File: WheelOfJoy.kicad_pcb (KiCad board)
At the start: 2 copper layers, 89.2 x 87.9 mm, 39 parts, among them CN1 JOY1, CN2 JOY2, CN3 JOY3, CN4 JOY4, CN5 JOY5, CN6 JOY6, CN7 JOY7, CN8 JOY8, CN9 DB15F, U1 CD4051B, U2 CD4051B, U3 CD4051B, U4 CD4051B, U5 CD4051B

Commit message: WIP
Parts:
- removed C4, C5: 100n, Capacitor_THT:C_Disc_D7.0mm_W2.5mm_P5.00mm
- removed CN5: JOY5, Connector_Dsub:DSUB-9_Male_EdgeMount_P2.77mm
- removed CN6: JOY6, Connector_Dsub:DSUB-9_Male_EdgeMount_P2.77mm
- removed CN7: JOY7, Connector_Dsub:DSUB-9_Male_EdgeMount_P2.77mm
- removed CN8: JOY8, Connector_Dsub:DSUB-9_Male_EdgeMount_P2.77mm
- removed RN9: 100, Resistor_THT:R_Array_SIP10
- removed U4, U5: CD4051B, Package_DIP:DIP-16_W7.62mm_Socket_LongPads
- removed V6: PORT5_NO, WheelOfJoy:port5
- removed V7: PORT6_NO, WheelOfJoy:port6
- removed V8: PORT7_NO, WheelOfJoy:port7
- removed V9: PORT8_NO, WheelOfJoy:port8
- C1, C2, C3: footprint Capacitor_THT:C_Disc_D7.0mm_W2.5mm_P5.00mm -> Capacitor_SMD:C_0805_2012Metric_Pad1.18x1.45mm_HandSolder; moved to B.Cu
- C6: footprint Capacitor_THT:CP_Radial_D6.3mm_P2.50mm -> Capacitor_SMD:C_1206_3216Metric_Pad1.33x1.80mm_HandSolder
- RN1, RN2, RN3, RN4, RN5, RN6: footprint Resistor_THT:R_Array_SIP6 -> Resistor_SMD:R_Array_Convex_4x0603; moved to B.Cu
- RN7, RN8: value 4.7k -> 100; footprint Resistor_THT:R_Array_SIP6 -> Resistor_SMD:R_Array_Convex_4x0603
- U1, U2, U3: value CD4051B -> 74LS153; footprint Package_DIP:DIP-16_W7.62mm_Socket_LongPads -> Package_SO:SOIC-16_3.9x9.9mm_P1.27mm; moved to B.Cu
- moved V5 80.0 mm to (166.0, 130.4)
- moved CN4 72.9 mm to (167.4, 121.2), turned to 77.2 degrees
- moved RN4 63.6 mm to (148.6, 124.4), turned to 180 degrees
- moved RN5 61.2 mm to (148.6, 119.2), turned to 180 degrees
- moved V4 61.1 mm to (166.8, 106.8)
- moved RN6 53.1 mm to (161.7, 121.2), turned to 180 degrees
- moved CN3 51.3 mm to (159.4, 100.4), turned to 144 degrees
- moved RN7 50.5 mm to (148.6, 126.9), turned to 90 degrees
- moved V0 43.8 mm to (148.8, 111.3)
- moved RN3 43.6 mm to (135.5, 121.2), turned to 180 degrees
- moved U2 41.0 mm to (141.8, 121.2), turned to 180 degrees
- moved RN8 40.4 mm to (140.1, 126.9), turned to 90 degrees
- moved C2 39.3 mm to (141.8, 114.2), turned to 0 degrees
- moved RN2 37.0 mm to (155.4, 106.4), turned to 180 degrees
- moved V3 35.4 mm to (146.4, 94.4)
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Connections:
- CN1 pad 9: (no net) -> Net-(CN1-Pad9)
- CN2 pad 9: (no net) -> Net-(CN2-Pad9)
- CN3 pad 9: (no net) -> Net-(CN3-Pad9)
- CN4 pad 9: (no net) -> Net-(CN4-Pad9)
- CN9 pad 11: /d5 -> Net-(CN9-Pad11)
- CN9 pad 14: (no net) -> Net-(CN9-Pad14)
- CN9 pad 6: (no net) -> /~reset
- CN9 pad 7: (no net) -> Net-(CN9-Pad7)
- RN1 pad 1: +5V -> Net-(CN4-Pad2)
- RN1 pad 2: Net-(CN1-Pad6) -> Net-(CN3-Pad2)
- RN1 pad 3: Net-(CN1-Pad4) -> Net-(CN2-Pad2)
- RN1 pad 4: Net-(CN1-Pad3) -> Net-(CN1-Pad2)
- RN1 pad 5: Net-(CN1-Pad2) -> +5V
- RN1 pad 6: Net-(CN1-Pad1) -> +5V
- RN2 pad 2: Net-(CN2-Pad6) -> +5V
- RN2 pad 3: Net-(CN2-Pad4) -> +5V
- RN2 pad 4: Net-(CN2-Pad3) -> +5V
- RN2 pad 5: Net-(CN2-Pad2) -> Net-(CN1-Pad1)
- RN3 pad 1: +5V -> Net-(CN4-Pad4)
- RN3 pad 2: Net-(CN3-Pad6) -> Net-(CN3-Pad4)
- RN3 pad 3: Net-(CN3-Pad4) -> Net-(CN2-Pad4)
- RN3 pad 4: Net-(CN3-Pad3) -> Net-(CN1-Pad4)
- RN3 pad 5: Net-(CN3-Pad2) -> +5V
- RN3 pad 6: Net-(CN3-Pad1) -> +5V
- RN4 pad 2: Net-(CN4-Pad6) -> +5V
- RN4 pad 3: Net-(CN4-Pad4) -> +5V
- RN4 pad 4: Net-(CN4-Pad3) -> +5V
- RN4 pad 5: Net-(CN4-Pad2) -> Net-(CN1-Pad3)
- RN4 pad 6: Net-(CN4-Pad1) -> Net-(CN2-Pad3)
- RN5 pad 1: +5V -> Net-(CN4-Pad9)
- RN5 pad 2: Net-(CN5-Pad6) -> Net-(CN3-Pad9)
- RN5 pad 3: Net-(CN5-Pad4) -> Net-(CN2-Pad9)
- RN5 pad 4: Net-(CN5-Pad3) -> Net-(CN1-Pad9)
- RN5 pad 5: Net-(CN5-Pad2) -> +5V
- RN5 pad 6: Net-(CN5-Pad1) -> +5V
- RN6 pad 2: Net-(CN6-Pad6) -> +5V
- RN6 pad 3: Net-(CN6-Pad4) -> +5V
- RN6 pad 4: Net-(CN6-Pad3) -> +5V
- RN6 pad 5: Net-(CN6-Pad2) -> Net-(CN1-Pad6)
- RN6 pad 6: Net-(CN6-Pad1) -> Net-(CN2-Pad6)
- RN7 pad 1: +5V -> Net-(RN7-Pad1)
- RN7 pad 3: Net-(CN7-Pad4) -> Net-(CN9-Pad11)
- RN7 pad 4: Net-(CN7-Pad3) -> Net-(CN9-Pad10)
- RN7 pad 5: Net-(CN7-Pad2) -> /d4
- RN7 pad 6: Net-(CN7-Pad1) -> /d5
- RN8 pad 1: +5V -> Net-(CN9-Pad5)
- RN8 pad 2: Net-(CN8-Pad6) -> Net-(CN9-Pad4)
- RN8 pad 3: Net-(CN8-Pad4) -> Net-(CN9-Pad3)
- RN8 pad 4: Net-(CN8-Pad3) -> Net-(CN9-Pad2)
- RN8 pad 5: Net-(CN8-Pad2) -> /d0
- RN8 pad 6: Net-(CN8-Pad1) -> /d1
- U1 pad 1: Net-(CN5-Pad1) -> GND
- U1 pad 10: /d6 -> Net-(CN1-Pad2)
- U1 pad 11: /d5 -> Net-(CN2-Pad2)
- U1 pad 12: Net-(CN4-Pad1) -> Net-(CN3-Pad2)
- U1 pad 13: Net-(CN1-Pad1) -> Net-(CN4-Pad2)
- U1 pad 14: Net-(CN2-Pad1) -> /d6
- U1 pad 15: Net-(CN3-Pad1) -> GND
- U1 pad 2: Net-(CN7-Pad1) -> /d7
- U1 pad 3: /d0 -> Net-(CN4-Pad1)
- U1 pad 4: Net-(CN8-Pad1) -> Net-(CN3-Pad1)
- U1 pad 5: Net-(CN6-Pad1) -> Net-(CN2-Pad1)
- U1 pad 6: GND -> Net-(CN1-Pad1)
- U1 pad 7: GND -> /d0
- U1 pad 9: /d7 -> /d1
- U2 pad 1: Net-(CN5-Pad2) -> GND
- U2 pad 10: /d6 -> Net-(CN1-Pad4)
- U2 pad 11: /d5 -> Net-(CN2-Pad4)
- U2 pad 12: Net-(CN4-Pad2) -> Net-(CN3-Pad4)
- U2 pad 13: Net-(CN1-Pad2) -> Net-(CN4-Pad4)
- U2 pad 14: Net-(CN2-Pad2) -> /d6
- U2 pad 15: Net-(CN3-Pad2) -> GND
- U2 pad 2: Net-(CN7-Pad2) -> /d7
- U2 pad 3: /d1 -> Net-(CN4-Pad3)
- U2 pad 4: Net-(CN8-Pad2) -> Net-(CN3-Pad3)
- U2 pad 5: Net-(CN6-Pad2) -> Net-(CN2-Pad3)
- U2 pad 6: GND -> Net-(CN1-Pad3)
- U2 pad 7: GND -> /d2
- U2 pad 9: /d7 -> /d3
- U3 pad 1: Net-(CN5-Pad3) -> GND
- U3 pad 10: /d6 -> Net-(CN1-Pad9)
- U3 pad 11: /d5 -> Net-(CN2-Pad9)
- U3 pad 12: Net-(CN4-Pad3) -> Net-(CN3-Pad9)
- U3 pad 13: Net-(CN1-Pad3) -> Net-(CN4-Pad9)
- U3 pad 14: Net-(CN2-Pad3) -> /d6
- U3 pad 15: Net-(CN3-Pad3) -> GND
- U3 pad 2: Net-(CN7-Pad3) -> /d7
- U3 pad 3: /d2 -> Net-(CN4-Pad6)
- U3 pad 4: Net-(CN8-Pad3) -> Net-(CN3-Pad6)
- U3 pad 5: Net-(CN6-Pad3) -> Net-(CN2-Pad6)
- U3 pad 6: GND -> Net-(CN1-Pad6)
- U3 pad 7: GND -> /d4
- U3 pad 9: /d7 -> /d5
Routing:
- net +5V: track 461.8 -> 66.4 mm, vias 6 -> 1
- net /d5: track 134.9 -> 0.00 mm, vias 2 -> 0
- net /d6: track 131.0 -> 0.00 mm, vias 2 -> 0
- net /d7: track 134.7 -> 14.2 mm, vias 1 -> 0
- net Net-(CN5-Pad6): track 84.9 -> 0.00 mm, vias 1 -> 0
- net Net-(CN1-Pad2): track 86.5 -> 3.99 mm, vias 1 -> 0
- net Net-(CN6-Pad6): track 81.6 -> 0.00 mm, vias 3 -> 0
- net Net-(CN7-Pad1): track 79.7 -> 0.00 mm, vias 1 -> 0
- net Net-(CN5-Pad3): track 79.0 -> 0.00 mm, vias 2 -> 0
- net Net-(CN6-Pad3): track 75.1 -> 0.00 mm, vias 1 -> 0
- net Net-(RN7-Pad2): track 74.6 -> 0.00 mm, vias 3 -> 0
- net Net-(CN8-Pad1): track 73.8 -> 0.00 mm, vias 1 -> 0
- net Net-(CN8-Pad3): track 67.6 -> 0.00 mm, vias 1 -> 0
- net Net-(CN3-Pad6): track 70.0 -> 3.05 mm, vias 1 -> 0
- net Net-(CN2-Pad2): track 69.1 -> 3.80 mm, vias 1 -> 0
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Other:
- board size 89.2 x 87.9 mm -> 47.8 x 45.4 mm

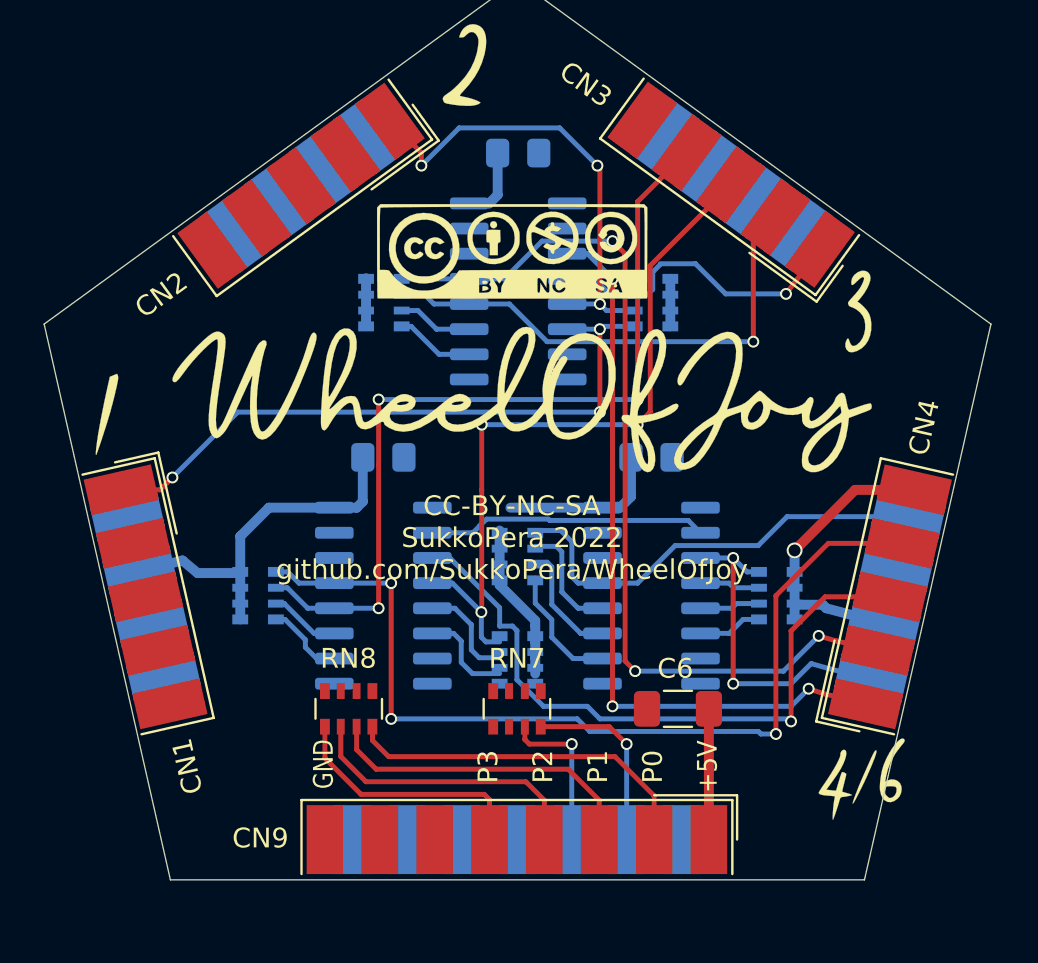
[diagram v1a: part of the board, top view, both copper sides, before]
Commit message: Restart routing from scratch
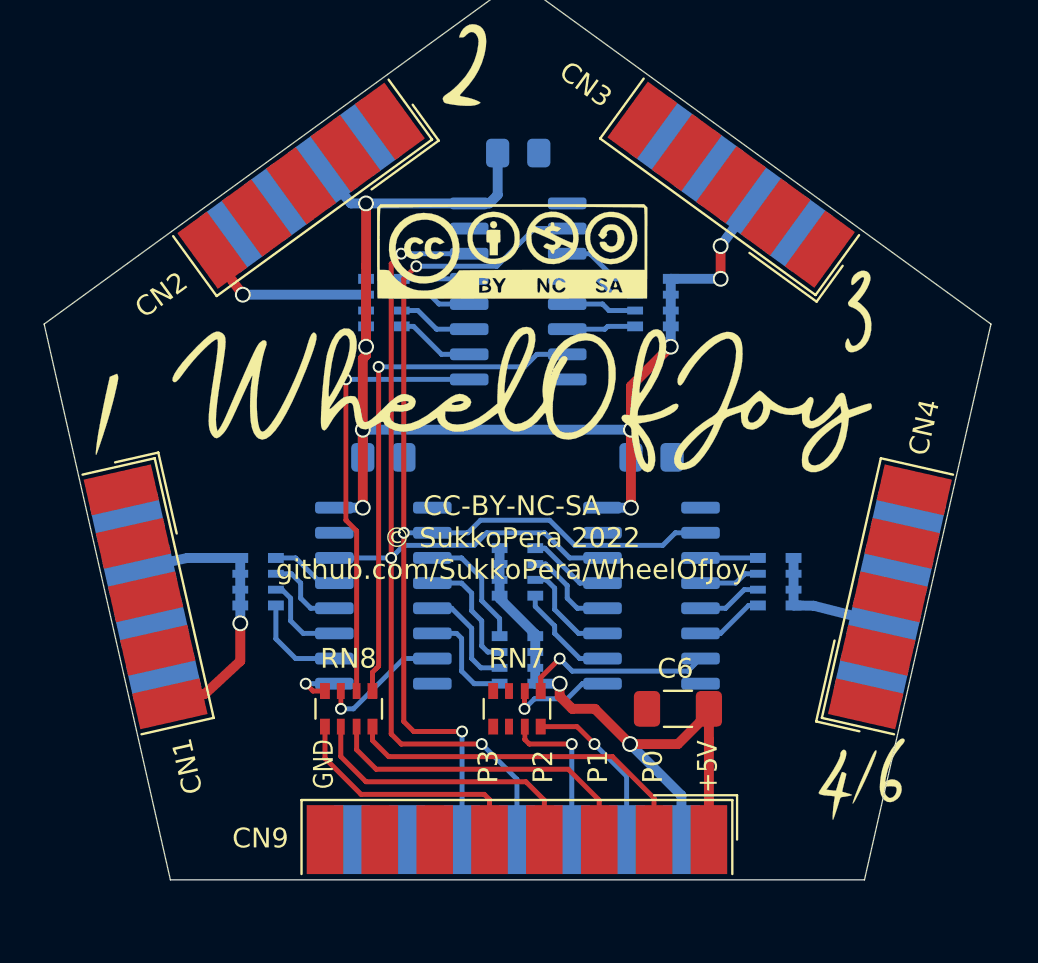
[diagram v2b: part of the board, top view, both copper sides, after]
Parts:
- moved RN5 0.77 mm to (148.6, 120.0)
- moved RN6 0.71 mm to (161.7, 120.5)
- moved RN3 0.70 mm to (135.5, 120.5)
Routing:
- net +5V: track 66.4 -> 132.0 mm, vias 1 -> 13
- net /d6: track 0.00 -> 52.8 mm, vias 0 -> 3
- net Net-(CN4-Pad4): track 47.1 -> 3.48 mm, vias 3 -> 0
- net Net-(CN4-Pad2): track 46.8 -> 3.41 mm, vias 3 -> 0
- net /d7: track 14.2 -> 56.3 mm, vias 0 -> 3
- net Net-(CN3-Pad4): track 42.9 -> 4.12 mm, vias 3 -> 0
- net Net-(CN4-Pad1): track 38.8 -> 3.96 mm, vias 3 -> 0
- net Net-(CN3-Pad3): track 36.8 -> 6.10 mm, vias 3 -> 0
- net Net-(CN1-Pad1): track 33.5 -> 3.49 mm, vias 3 -> 0
- net Net-(CN4-Pad3): track 33.8 -> 6.22 mm, vias 1 -> 0
- net /d0: track 0.00 -> 26.3 mm, vias 0 -> 1
- net /d1: track 0.00 -> 22.2 mm, vias 0 -> 1
- net Net-(CN3-Pad2): track 25.5 -> 3.60 mm, vias 1 -> 0
- net Net-(CN2-Pad1): track 24.0 -> 3.57 mm, vias 3 -> 0
- net Net-(CN4-Pad9): track 22.4 -> 4.13 mm
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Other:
- board text added: "CC-BY-NC-SA © SukkoPera 2022 github.com/SukkoPera/WheelOfJoy"
- board text removed: "CC-BY-NC-SA SukkoPera 2022 github.com/SukkoPera/WheelOfJoy"

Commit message: WIP
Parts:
- removed C2, C3: 100n, Capacitor_SMD:C_0805_2012Metric_Pad1.18x1.45mm_HandSolder
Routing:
- net +5V: track 132.0 -> 177.5 mm, vias 13 -> 23
- net Net-(CN1-Pad9): track 5.25 -> 50.2 mm, vias 0 -> 4
- net GND: track 0.00 -> 43.9 mm, vias 0 -> 6
- net Net-(CN3-Pad4): track 4.12 -> 47.8 mm, vias 0 -> 3
- net Net-(CN1-Pad6): track 3.54 -> 43.0 mm, vias 0 -> 6
- net Net-(CN4-Pad2): track 3.41 -> 42.7 mm, vias 0 -> 3
- net Net-(CN2-Pad6): track 3.34 -> 42.0 mm, vias 0 -> 4
- net Net-(CN4-Pad4): track 3.48 -> 41.7 mm, vias 0 -> 3
- net Net-(CN4-Pad3): track 6.22 -> 43.1 mm, vias 0 -> 3
- net Net-(CN3-Pad3): track 6.10 -> 38.6 mm, vias 0 -> 3
- net Net-(CN2-Pad9): track 5.15 -> 37.6 mm, vias 0 -> 4
- net Net-(CN4-Pad1): track 3.96 -> 36.3 mm, vias 0 -> 3
- net Net-(CN1-Pad1): track 3.49 -> 33.9 mm, vias 0 -> 3
- net Net-(CN2-Pad3): track 5.54 -> 34.4 mm, vias 0 -> 3
- net Net-(CN1-Pad3): track 5.42 -> 33.0 mm, vias 0 -> 3
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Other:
- net class Default: clearance 0.2 -> 0.15; trace_width 0.25 -> 0.16; via_dia 0.6 -> 0.3; via_drill 0.4 -> 0.25
- net class Power: clearance 0.2 -> 0.15
- rule trace_clearance: 0.2 -> 0.15
- rule trace_min: 0.2 -> 0.127
- rule via_min_drill: 0.3 -> 0.25
- rule via_min_size: 0.4 -> 0.3

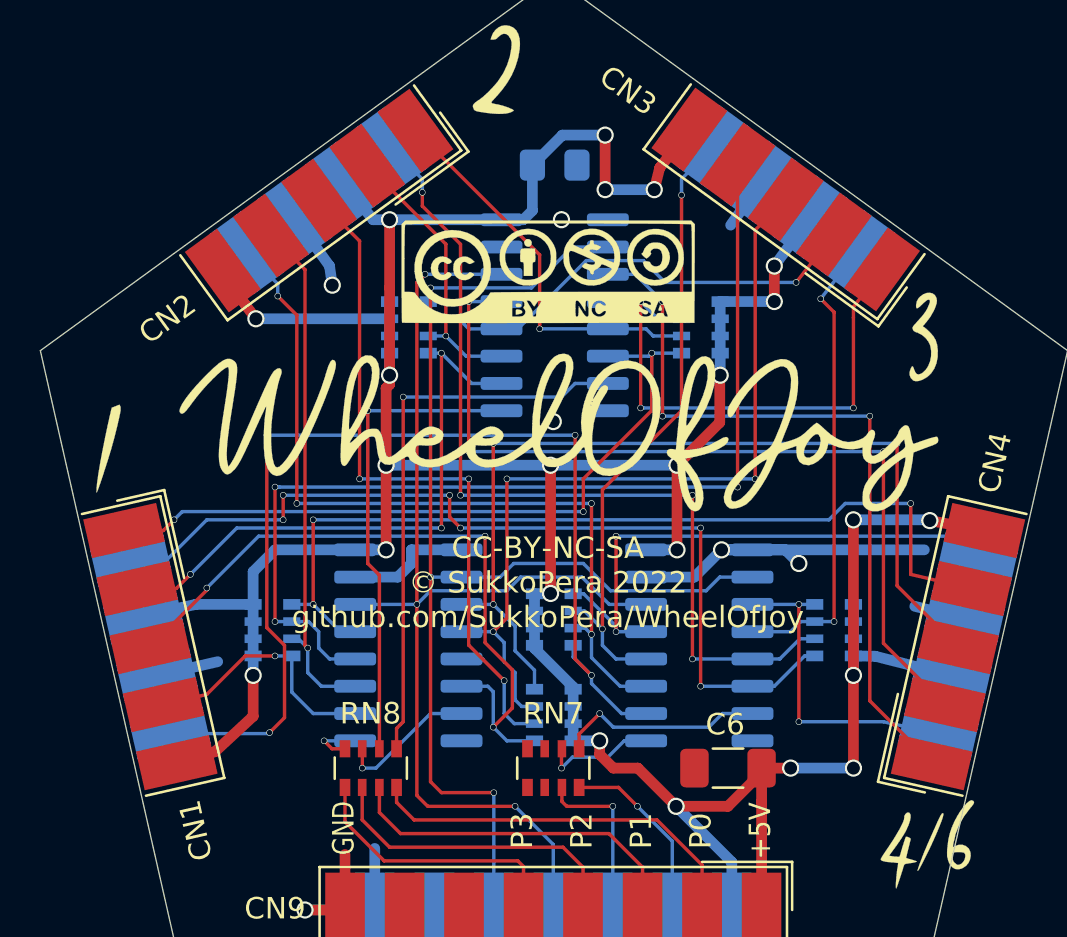
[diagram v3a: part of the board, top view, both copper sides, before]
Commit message: Honing tracks
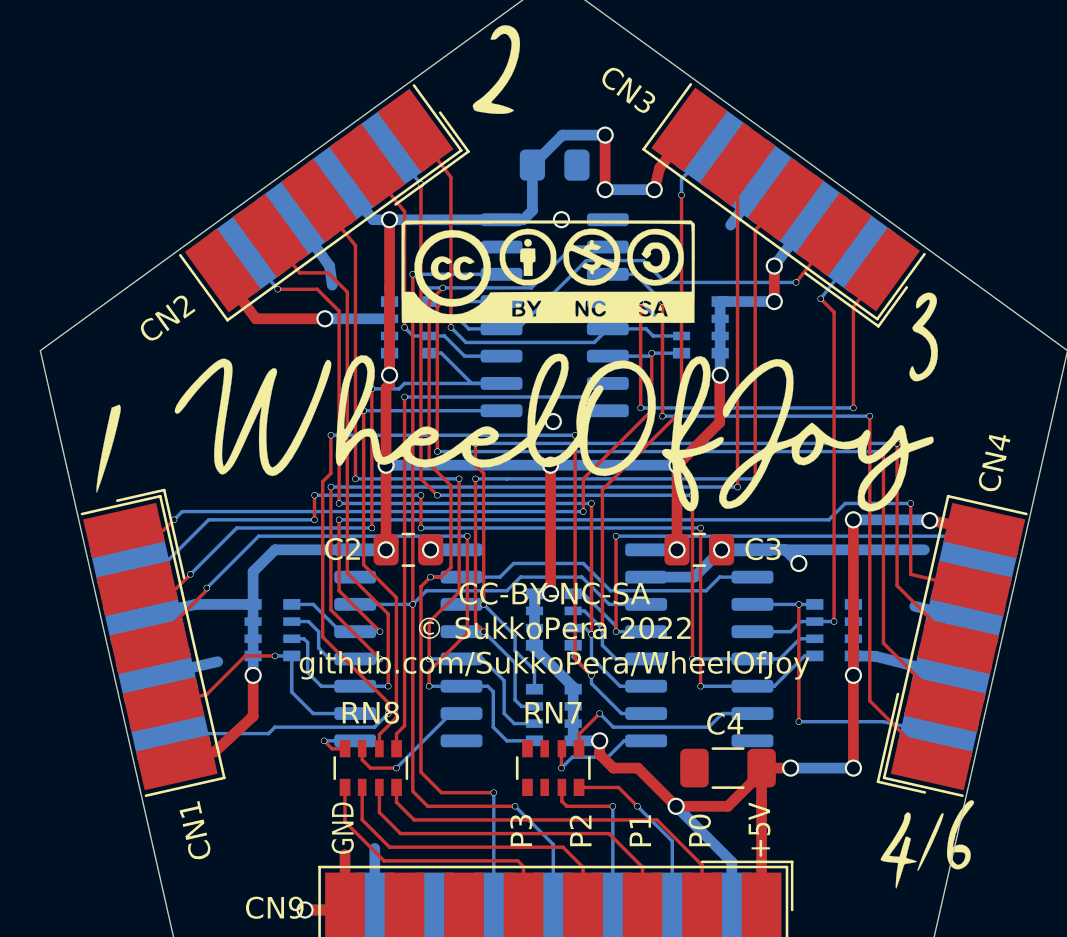
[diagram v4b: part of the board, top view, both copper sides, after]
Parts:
- added C2: 100n, Capacitor_SMD:C_0805_2012Metric_Pad1.18x1.45mm_HandSolder, F.Cu at (141.8, 116.7)
- added C3: 100n, Capacitor_SMD:C_0805_2012Metric_Pad1.18x1.45mm_HandSolder, F.Cu at (155.4, 116.7)
- moved V0 0.22 mm to (148.6, 111.3)
- renumbered C6 to C4
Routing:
- net GND: track 43.9 -> 38.0 mm
- net Net-(CN2-Pad4): track 24.4 -> 30.1 mm
- net Net-(CN1-Pad9): track 50.2 -> 53.0 mm
- net Net-(CN2-Pad1): track 18.4 -> 21.1 mm
- net /d7: track 56.7 -> 58.9 mm
- net Net-(CN4-Pad4): track 41.7 -> 43.7 mm
- net Net-(CN4-Pad2): track 42.7 -> 44.2 mm
- net Net-(CN1-Pad3): track 33.0 -> 31.6 mm
- net Net-(CN1-Pad2): track 27.5 -> 28.7 mm
- net Net-(CN3-Pad3): track 38.6 -> 39.7 mm
- net /d1: track 22.2 -> 23.1 mm
- net Net-(CN4-Pad3): track 43.1 -> 43.9 mm
- net Net-(CN2-Pad6): track 42.0 -> 42.6 mm

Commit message: Another port done
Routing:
- net Net-(CN1-Pad4): track 11.8 -> 32.5 mm, vias 1 -> 3
- net Net-(CN1-Pad9): track 53.0 -> 48.6 mm, vias 4 -> 6
- net Net-(CN1-Pad6): track 43.3 -> 40.3 mm, vias 6 -> 2
- net Net-(CN1-Pad3): track 31.6 -> 33.9 mm
- net Net-(CN1-Pad2): track 28.7 -> 29.5 mm
- net +5V: track 177.6 -> 178.2 mm

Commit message: Another one
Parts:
- C1: moved to F.Cu
- moved C1 2.54 mm to (148.7, 101.3)
- moved V1 1.42 mm to (148.6, 105.2)
- moved V0 0.76 mm to (148.6, 112.0)
- moved V4 0.57 mm to (167.3, 106.6)
- moved V3 0.51 mm to (146.4, 94.9)
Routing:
- net Net-(CN3-Pad1): track 25.5 -> 15.8 mm
- net GND: track 38.0 -> 30.0 mm
- net Net-(CN2-Pad9): track 37.4 -> 44.1 mm
- net Net-(CN1-Pad9): track 48.6 -> 54.8 mm
- net Net-(CN3-Pad6): track 22.1 -> 28.0 mm
- net Net-(CN4-Pad6): track 15.0 -> 20.3 mm
- net Net-(CN1-Pad1): track 33.9 -> 37.2 mm
- net Net-(CN3-Pad9): track 29.3 -> 32.6 mm
- net Net-(CN3-Pad4): track 48.3 -> 45.2 mm
- net Net-(CN4-Pad4): track 43.7 -> 41.2 mm
- net Net-(CN1-Pad2): track 29.5 -> 27.2 mm
- net Net-(CN4-Pad9): track 26.0 -> 28.2 mm
- net Net-(CN3-Pad3): track 39.7 -> 37.8 mm
- net Net-(CN4-Pad1): track 36.3 -> 37.6 mm
- net Net-(CN2-Pad6): track 42.6 -> 43.3 mm
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
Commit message: Almost there
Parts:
- moved RN1 1.28 mm to (141.7, 105.1)
- moved RN2 1.27 mm to (155.5, 105.1)
- moved C1 1.27 mm to (148.7, 100.1)
- moved U1 1.27 mm to (148.7, 104.5)
- moved V1 1.08 mm to (148.6, 104.1)
- moved V0 0.63 mm to (148.6, 111.4)
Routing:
- net Net-(CN4-Pad2): track 44.2 -> 45.5 mm
- net /d0: track 26.3 -> 27.5 mm
- net Net-(CN2-Pad2): track 13.2 -> 11.9 mm
- net Net-(CN1-Pad2): track 27.2 -> 28.5 mm
- net Net-(CN2-Pad1): track 21.1 -> 19.9 mm
- net Net-(CN4-Pad1): track 37.6 -> 38.9 mm
- net /d1: track 23.1 -> 24.4 mm
- net Net-(CN1-Pad1): track 37.2 -> 38.5 mm
- net /d6: track 53.3 -> 54.2 mm
- net +5V: track 178.7 -> 178.0 mm

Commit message: Update silkscreen
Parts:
- moved V5 0.57 mm to (165.7, 130.9)
- moved V3 0.28 mm to (146.6, 95.1)
- renumbered CN9 to CN5
